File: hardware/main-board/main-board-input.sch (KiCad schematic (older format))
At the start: 26 parts, among them SW1 Start, SW10 Menu, SW2 Focus, SW3 Inc Exposure, SW4 Dec Exposure, SW5 Inc Contrast, SW6 Dec Contrast, SW7 Test Strip, SW8 Add Adjustment, SW9 Cancel

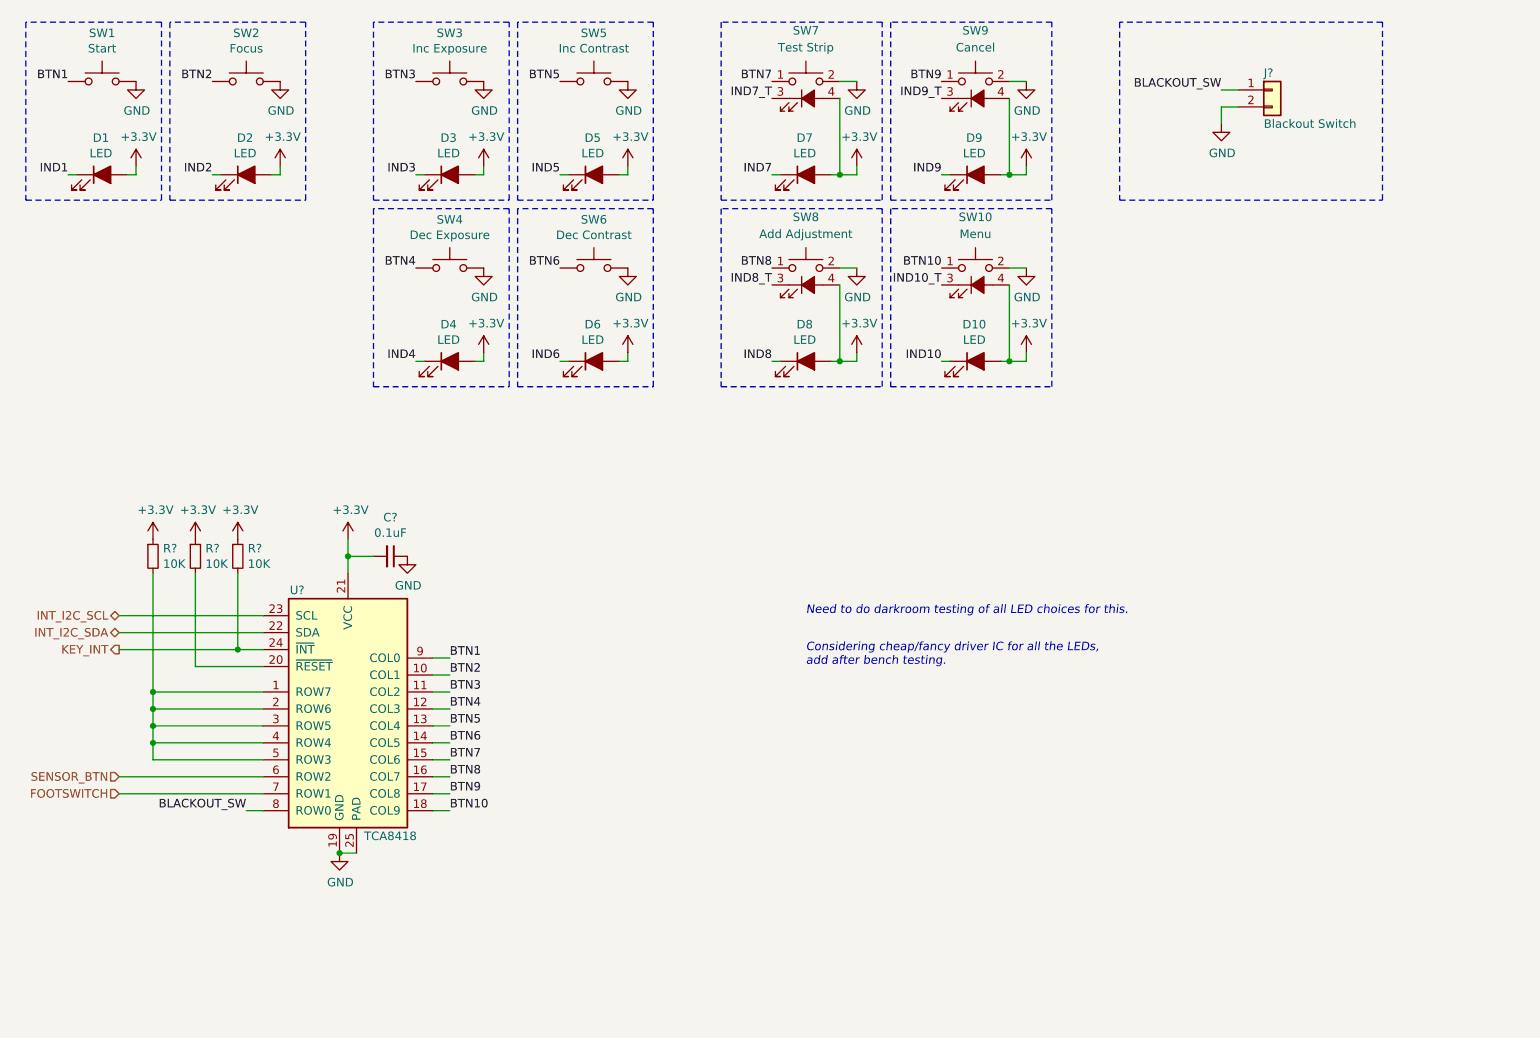
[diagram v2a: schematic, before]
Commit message: Added LED driver to schematics
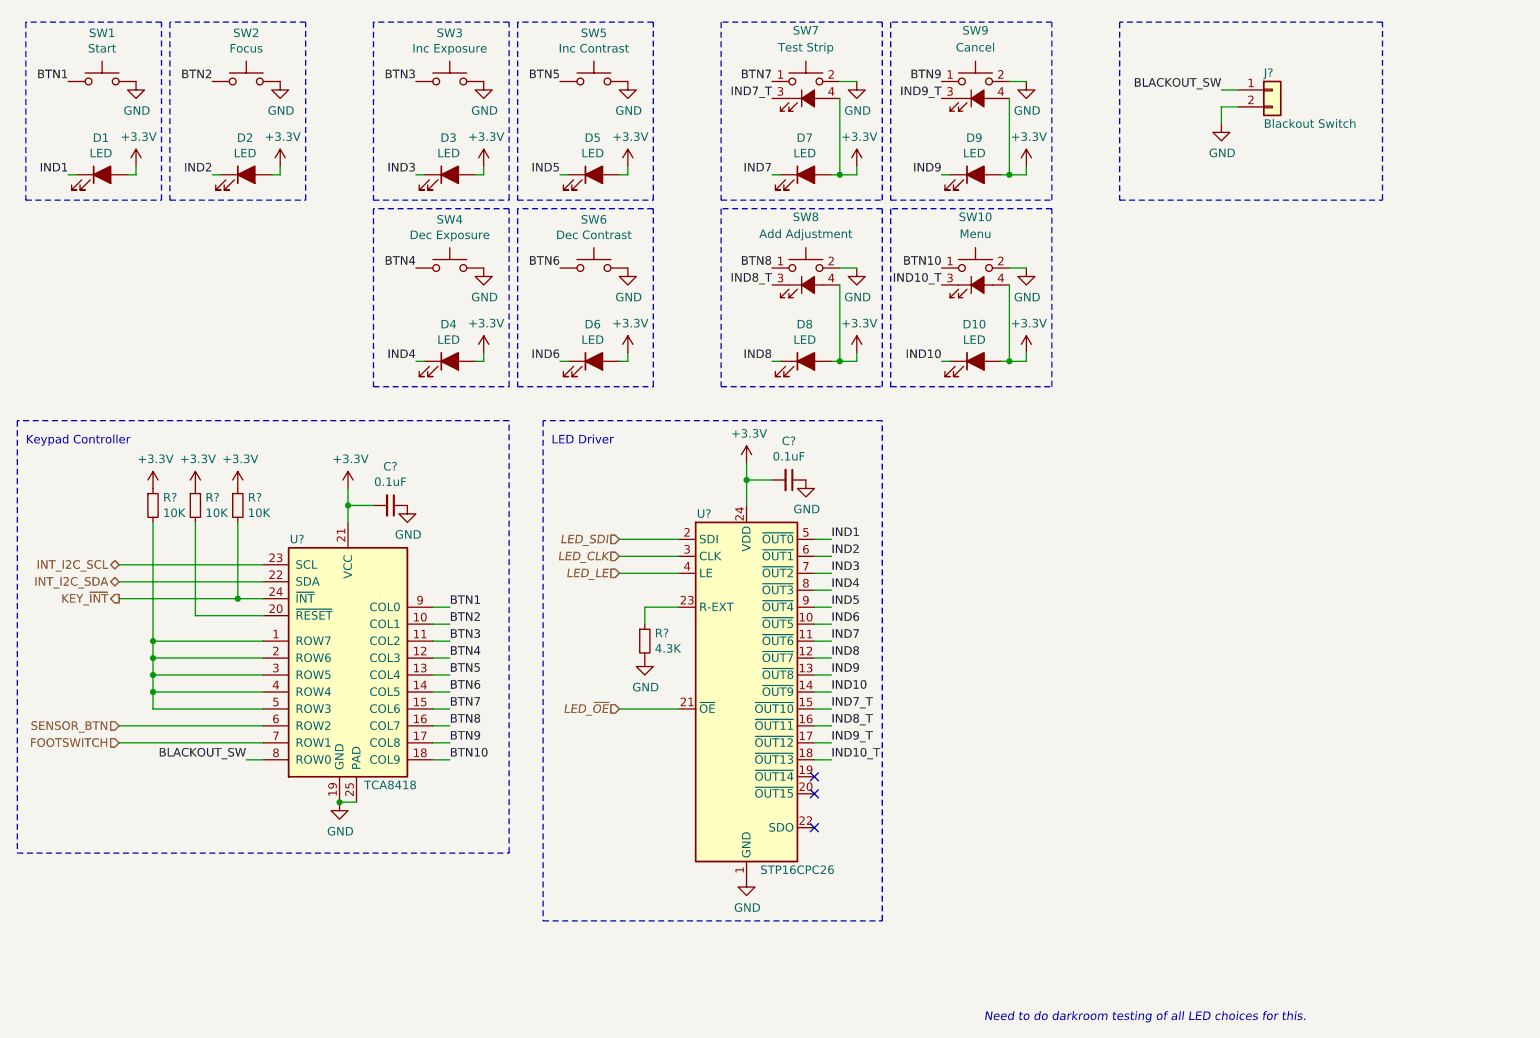
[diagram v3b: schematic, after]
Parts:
- added C?: 0.1uF, symbol Device:C_Small
- added R?: 4.3K, symbol Device:R_Small
- added U?: STP16CPC26, Package_SO:TSSOP-24_4.4x7.8mm_P0.65mm, symbol Project:STP16CPC26
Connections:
- net +3V3: now also C?.2, U?.24 (VDD)
- net GND: now also C?.1, R?.2, U?.1 (GND)
- net IND1: now also U?.5 (~OUT0)
- net IND10: now also U?.14 (~OUT9)
- net IND10_T: now also U?.18 (~OUT13)
- net IND2: now also U?.6 (~OUT1)
- net IND3: now also U?.7 (~OUT2)
- net IND4: now also U?.8 (~OUT3)
- net IND5: now also U?.9 (~OUT4)
- net IND6: now also U?.10 (~OUT5)
- net IND7: now also U?.11 (~OUT6)
- net IND7_T: now also U?.15 (~OUT10)
- net IND8: now also U?.12 (~OUT7)
- net IND8_T: now also U?.16 (~OUT11)
- net IND9: now also U?.13 (~OUT8)
- net IND9_T: now also U?.17 (~OUT12)
- net KEY_INT renamed KEY_~INT
- new net: R?.1, U?.23 (R-EXT)
- new net LED_CLK: U?.3 (CLK)
- new net LED_LE: U?.4 (LE)
- new net LED_SDI: U?.2 (SDI)
- new net LED_~OE: U?.21 (~OE)
- no-connect marks 0 -> 3
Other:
- note added: "Keypad Controller"
- note added: "LED Driver"
- note removed: "Considering cheap/fancy driver IC for all the LEDs,\nadd after bench testing."
- moved on the sheet: C?, R?, U?

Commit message: Annotated schematic got ERC to pass
Annotated a few components manually, then let KiCad to the rest
automatically.

Added no-connection flags to all intentionally-unused pins.
Added comments next to no-connection pins that are likely to become used
soon.
Fixed USB power switch schematic symbol's output pin type.
Fixed IEC output jack schematic symbol pin types.
Rearranged power flags as needed to get ERC to pass.

In cases where power needs to flow through another component (switch,
fuse, inductor, etc) a power flag is needed to make ERC happy.

The Vcap pin on the STM32 schematic symbol seems to be designated as a
power input, even though this pin is only supposed to connect to a
capacitor to ground. Added a power flag to make ERC happy here, to avoid
duplicating a library symbol.
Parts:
- gave numbers to parts that had none: 9

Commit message: Fill in BOM data for all known components
Added BOM assignments for main board components
Fixed GNDDetect connection on STDC14 connector

Added more notes to the main board schematic of things that are still
TBD or need fixing.
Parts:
- C24, C25: footprint (none) -> Capacitor_SMD:C_0603_1608Metric; Description (none) -> CAP CER 0.1UF 25V X7R 0603; Manufacturer (none) -> Samsung Electro-Mechanics; Manufacturer PN (none) -> CL10B104KA8NNNC; Supplier (none) -> Digi-Key; Supplier PN (none) -> 1276-1006-1-ND
- D1, D10, D2, D3, D4, D5, D6, D7, D8, D9: footprint (none) -> LED_THT:LED_D5.0mm; Description (none) -> LED RED DIFFUSED T-1 3/4 T/H; Manufacturer (none) -> Lite-On Inc.; Manufacturer PN (none) -> LTL-4223; Supplier (none) -> Digi-Key; Supplier PN (none) -> 160-1127-ND
- J4: footprint Connector_PinHeader_2.54mm:PinHeader_1x02_P2.54mm_Vertical -> Connector_JST:JST_PH_B2B-PH-K_1x02_P2.00mm_Vertical; Description (none) -> CONN HEADER VERT 2POS 2MM; Manufacturer (none) -> JST Sales America Inc.; Manufacturer PN (none) -> B2B-PH-K-S(LF)(SN); Supplier (none) -> Digi-Key; Supplier PN (none) -> 455-1704-ND
- R5, R6, R7: footprint (none) -> Resistor_SMD:R_0603_1608Metric; Description (none) -> RES SMD 10K OHM 5% 1/10W 0603; Manufacturer (none) -> Vishay Dale; Manufacturer PN (none) -> CRCW060310K0JNEA; Supplier (none) -> Digi-Key; Supplier PN (none) -> 541-10KGCT-ND
- R8: footprint (none) -> Resistor_SMD:R_0603_1608Metric; Description (none) -> RES SMD 4.3K OHM 5% 1/10W 0603; Manufacturer (none) -> Vishay Dale; Manufacturer PN (none) -> CRCW06034K30JNEA; Supplier (none) -> Digi-Key; Supplier PN (none) -> 541-4.3KGCT-ND
- SW1, SW2: Description (none) -> PUSHBUTTON SPNO; Manufacturer (none) -> Marquardt Switches; Manufacturer PN (none) -> 6425.1101; Supplier (none) -> Mouser; Supplier PN (none) -> 979-6425.1101
- SW10, SW7, SW8, SW9: Description (none) -> PUSHBUTTON SPNO RED LED; Manufacturer (none) -> Marquardt Switches; Manufacturer PN (none) -> 6425.3111; Supplier (none) -> Mouser; Supplier PN (none) -> 979-6425.3111
- SW3, SW4, SW5, SW6: Description (none) -> PUSHBUTTON SPNO; Manufacturer (none) -> Marquardt Switches; Manufacturer PN (none) -> 6425.0101; Supplier (none) -> Mouser; Supplier PN (none) -> 979-6425.0101
- U7: Description (none) -> IC KEYPAD SCAN DEVICE I2C 24WQFN; Manufacturer (none) -> Texas Instruments; Manufacturer PN (none) -> TCA8418RTWR; Supplier (none) -> Digi-Key; Supplier PN (none) -> 296-25223-1-ND

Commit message: Added rotary encoder
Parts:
- added C28, C29: 0.01uF, Capacitor_SMD:C_0603_1608Metric, symbol Device:C_Small
- added R21, R22, R23, R4: 10K, Resistor_SMD:R_0603_1608Metric, symbol Device:R_Small
- added SW11: Rotary Encoder, lib_fp:RotaryEncoder_CUI_ACZ11BR1E-Switch_Vertical_H15mm, symbol Device:Rotary_Encoder_Switch
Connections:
- net +3V3: now also R22.1, R4.1
- net BLACKOUT_SW: now also U7.7 (ROW1); no longer U7.8 (ROW0)
- net FOOTSWITCH: now also U7.6 (ROW2); no longer U7.7 (ROW1)
- net GND: now also C28.2, C29.2, SW11.C, SW11.S2
- net SENSOR_BTN: now also U7.5 (ROW3); no longer U7.6 (ROW2)
- net at R5.2, U7.1 (ROW7), U7.2 (ROW6)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: no longer U7.5 (ROW3)
- new net: R21.2, R4.2, SW11.A
- new net: R22.2, R23.2, SW11.B
- new net ENC_A: C28.1, R21.1
- new net ENC_B: C29.1, R23.1
- new net ENC_BTN: SW11.S1, U7.8 (ROW0)
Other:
- moved on the sheet: J4

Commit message: Filled out BOM data for encoder filtering
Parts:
- C28, C29: Description (none) -> CAP CER 10000PF 25V X7R 0603; Manufacturer (none) -> Samsung Electro-Mechanics; Manufacturer PN (none) -> CL10B103KA8NNNC; Supplier (none) -> Digi-Key; Supplier PN (none) -> 1276-1132-1-ND
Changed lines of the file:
@@
 F 1 "0.01uF" H 7742 1555 50  0000 L CNN
 F 2 "Capacitor_SMD:C_0603_1608Metric" H 7650 1600 50  0001 C CNN
-F 3 "~" H 7650 1600 50  0001 C CNN
+F 3 "https://media.digikey.com/pdf/Data%20Sheets/Samsung%20PDFs/CL_Series_MLCC_ds.pdf" H 7650 1600 50  0001 C CNN
+F 4 "CAP CER 10000PF 25V X7R 0603" H 7650 1600 50  0001 C CNN "Description"
+F 5 "Samsung Electro-Mechanics" H 7650 1600 50  0001 C CNN "Manufacturer"
+F 6 "CL10B103KA8NNNC" H 7650 1600 50  0001 C CNN "Manufacturer PN"
+F 7 "Digi-Key" H 7650 1600 50  0001 C CNN "Supplier"
+F 8 "1276-1132-1-ND" H 7650 1600 50  0001 C CNN "Supplier PN"
 	1    7650 1600
 	1    0    0    -1
@@
 F 1 "0.01uF" H 7742 2455 50  0000 L CNN
 F 2 "Capacitor_SMD:C_0603_1608Metric" H 7650 2500 50  0001 C CNN
-F 3 "~" H 7650 2500 50  0001 C CNN
+F 3 "https://media.digikey.com/pdf/Data%20Sheets/Samsung%20PDFs/CL_Series_MLCC_ds.pdf" H 7650 2500 50  0001 C CNN
+F 4 "CAP CER 10000PF 25V X7R 0603" H 7650 2500 50  0001 C CNN "Description"
+F 5 "Samsung Electro-Mechanics" H 7650 2500 50  0001 C CNN "Manufacturer"
+F 6 "CL10B103KA8NNNC" H 7650 2500 50  0001 C CNN "Manufacturer PN"
+F 7 "Digi-Key" H 7650 2500 50  0001 C CNN "Supplier"
+F 8 "1276-1132-1-ND" H 7650 2500 50  0001 C CNN "Supplier PN"
 	1    7650 2500
 	1    0    0    -1

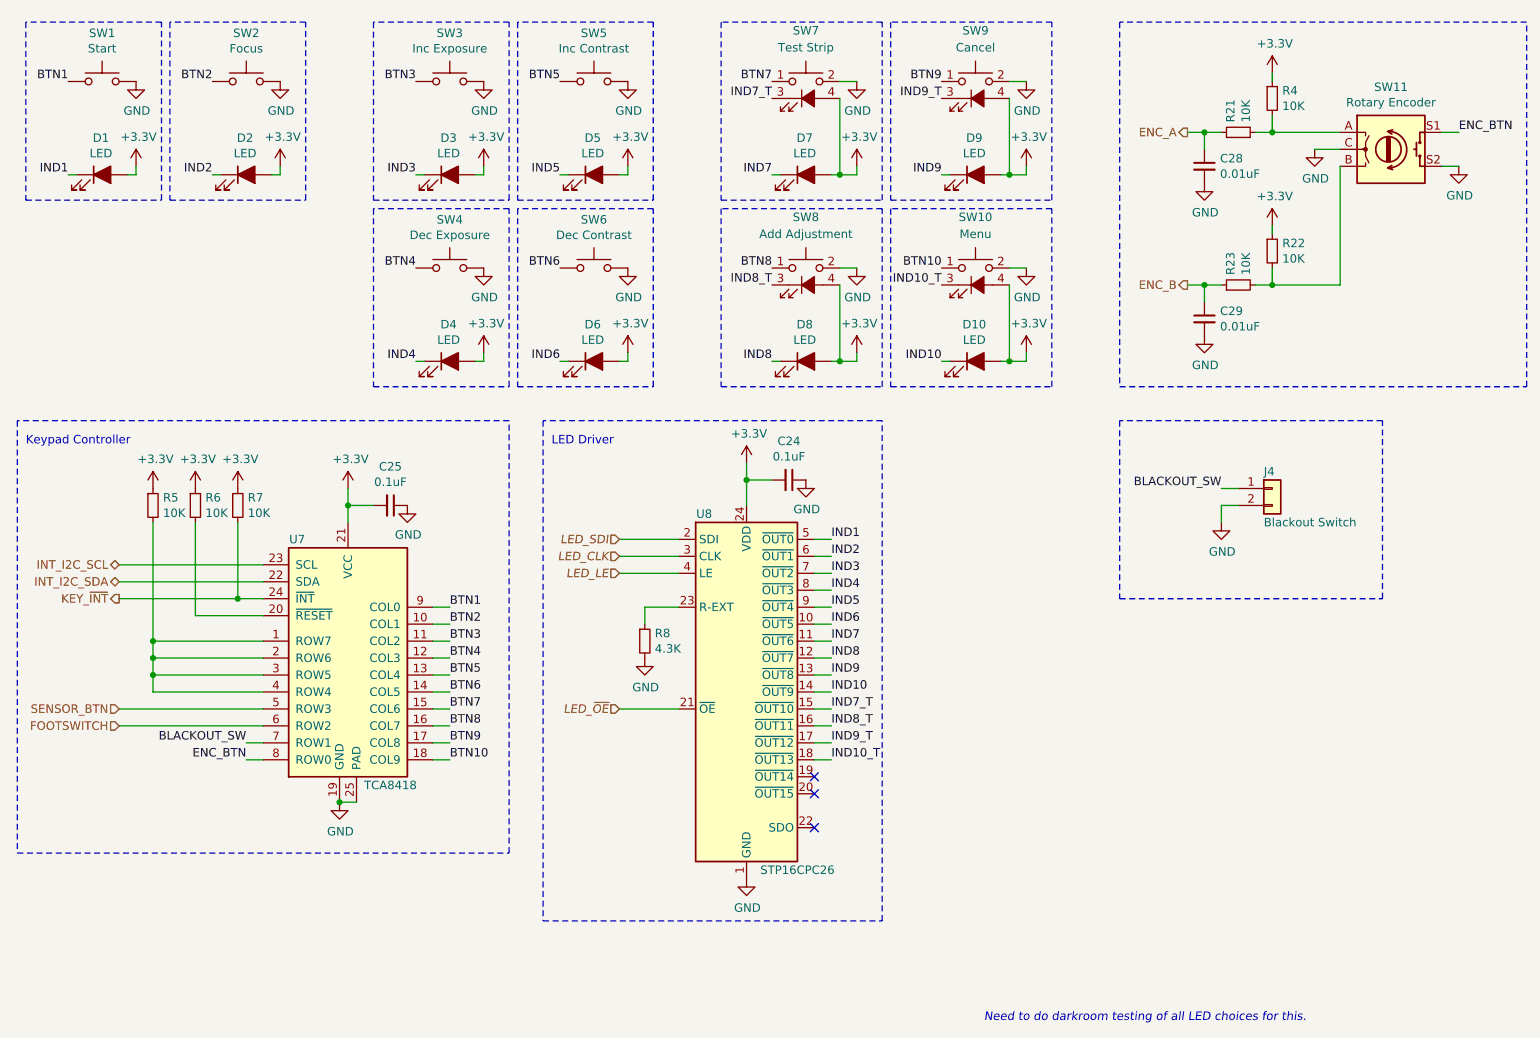
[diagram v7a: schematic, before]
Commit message: Main board schematic cleanup pass
Added mounting holes for the board and the OLED module
Connected GND and Earth nets
Cleaned up and labeled many parts of the schematic
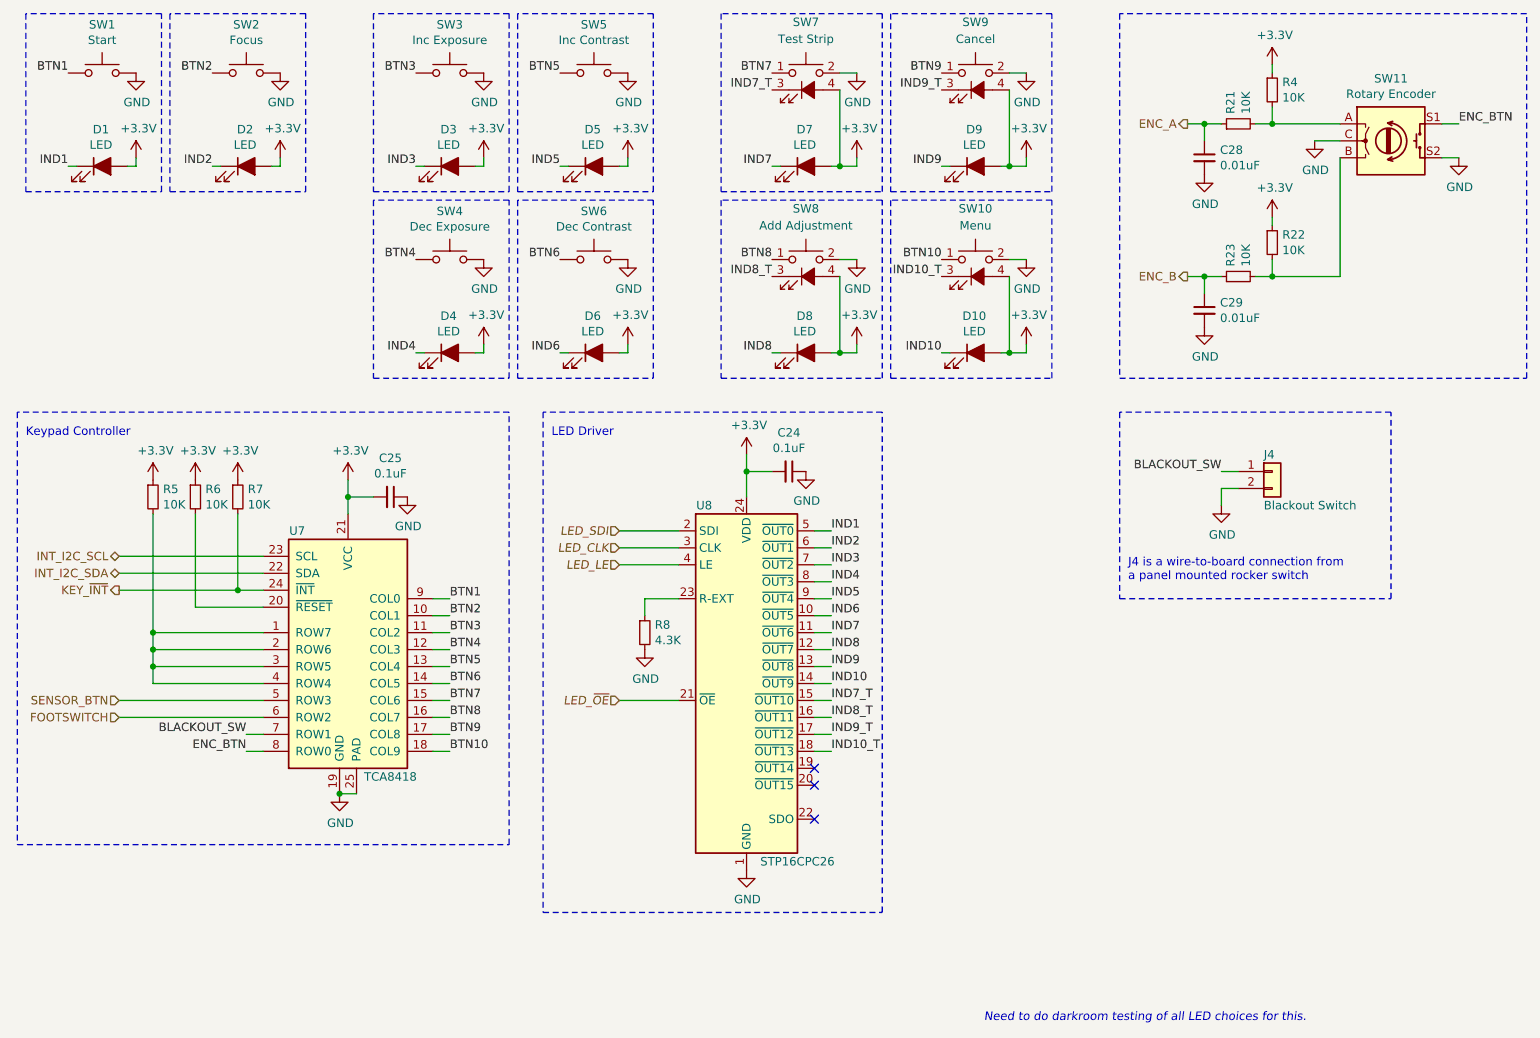
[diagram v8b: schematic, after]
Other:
- note added: "J4 is a wire-to-board connection from\na panel mounted rocker switch"
- moved on the sheet: C24, C25, C28, C29, D1, D10, D2, D3, D4, D5, D6, D7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
